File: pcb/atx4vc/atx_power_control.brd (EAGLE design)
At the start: 86 x 70 mm, 59 parts, among them IC2 REG1117, IC3 STM32F042F4, IC4 MY_7905DT, J1 ATX24RH, SW1 324_SW, SW2 324_SW, SW3 324_SW, SW4 324_SW, SW5 324_SW, SW7 324_SW, U1 USBC_16P, U2 USBC_16P

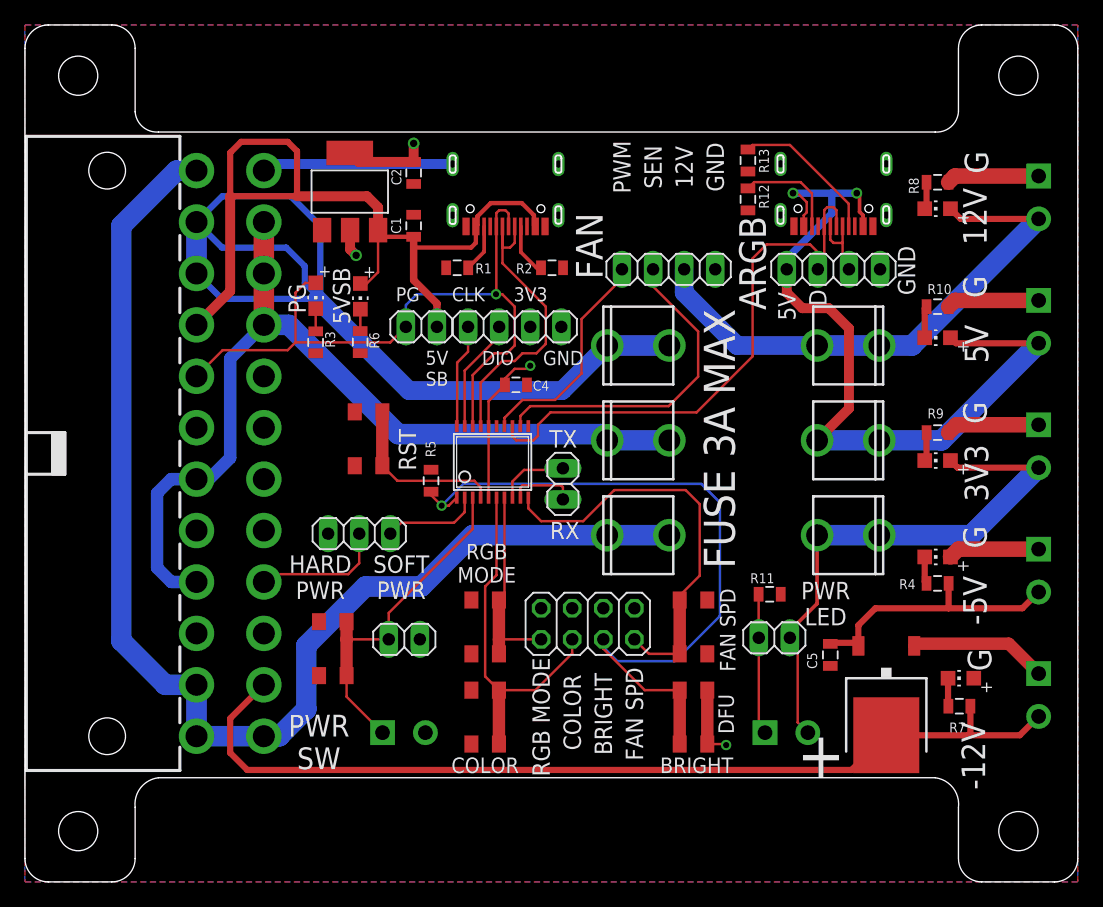
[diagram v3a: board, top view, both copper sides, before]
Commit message: adjusted fuse holder on PCB
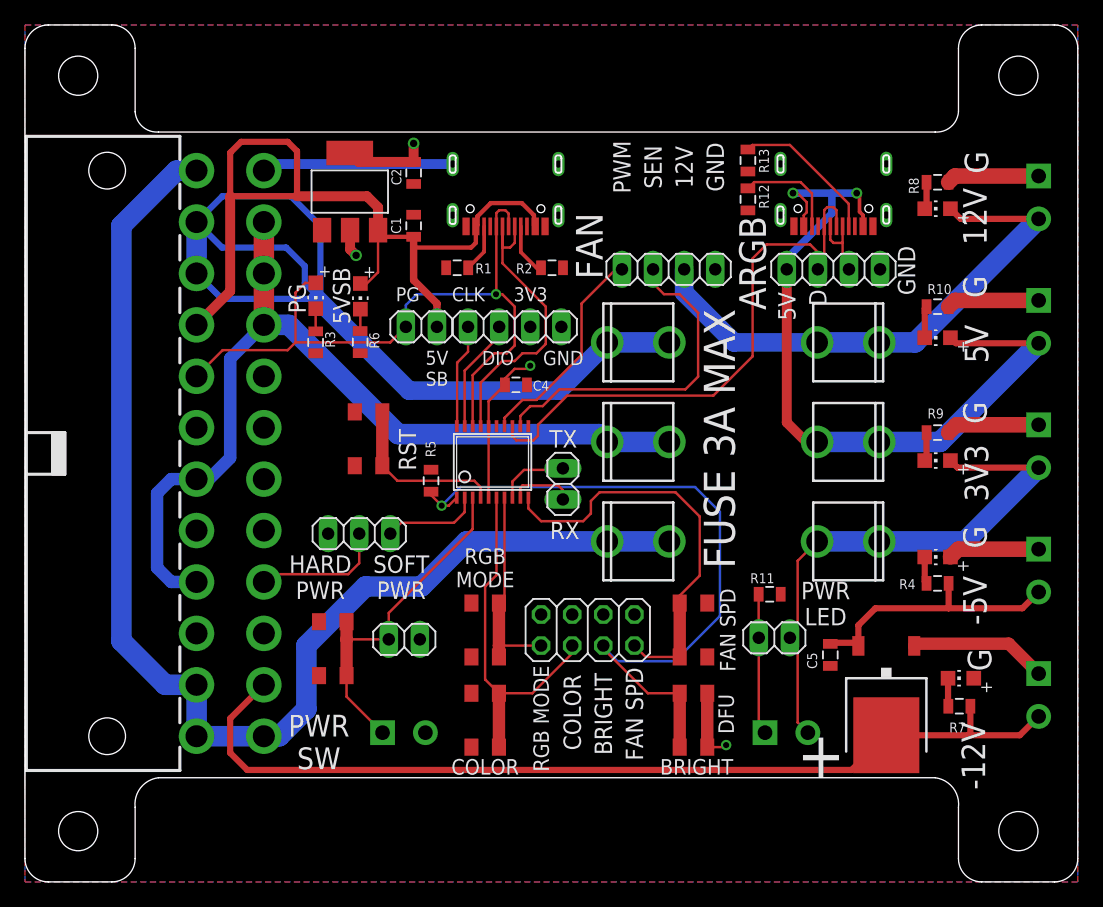
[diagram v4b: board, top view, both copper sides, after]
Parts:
- moved F3 0.51 mm to (58.7, 27.8)
- moved JP9 0.51 mm to (46.0, 20.6)
- moved F2 0.25 mm to (58.7, 44.1)
- moved SW2 0.25 mm to (37.6, 13.2)
- moved SW4 0.25 mm to (54.6, 13.2)
- moved SW5 0.25 mm to (37.6, 20.6)
- moved SW7 0.25 mm to (54.6, 20.6)
- moved F1 0.13 mm to (58.7, 35.9)
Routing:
- net N$15: track 66.6 -> 63.8 mm
- net BUTTON2: track 61.3 -> 59.8 mm
- net N$6: track 27.0 -> 27.7 mm
- net N$7: track 18.4 -> 17.8 mm
